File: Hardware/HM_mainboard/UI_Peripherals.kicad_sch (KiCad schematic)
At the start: 20 parts, among them J4 FC68125, U3 WE-TVS-824015043

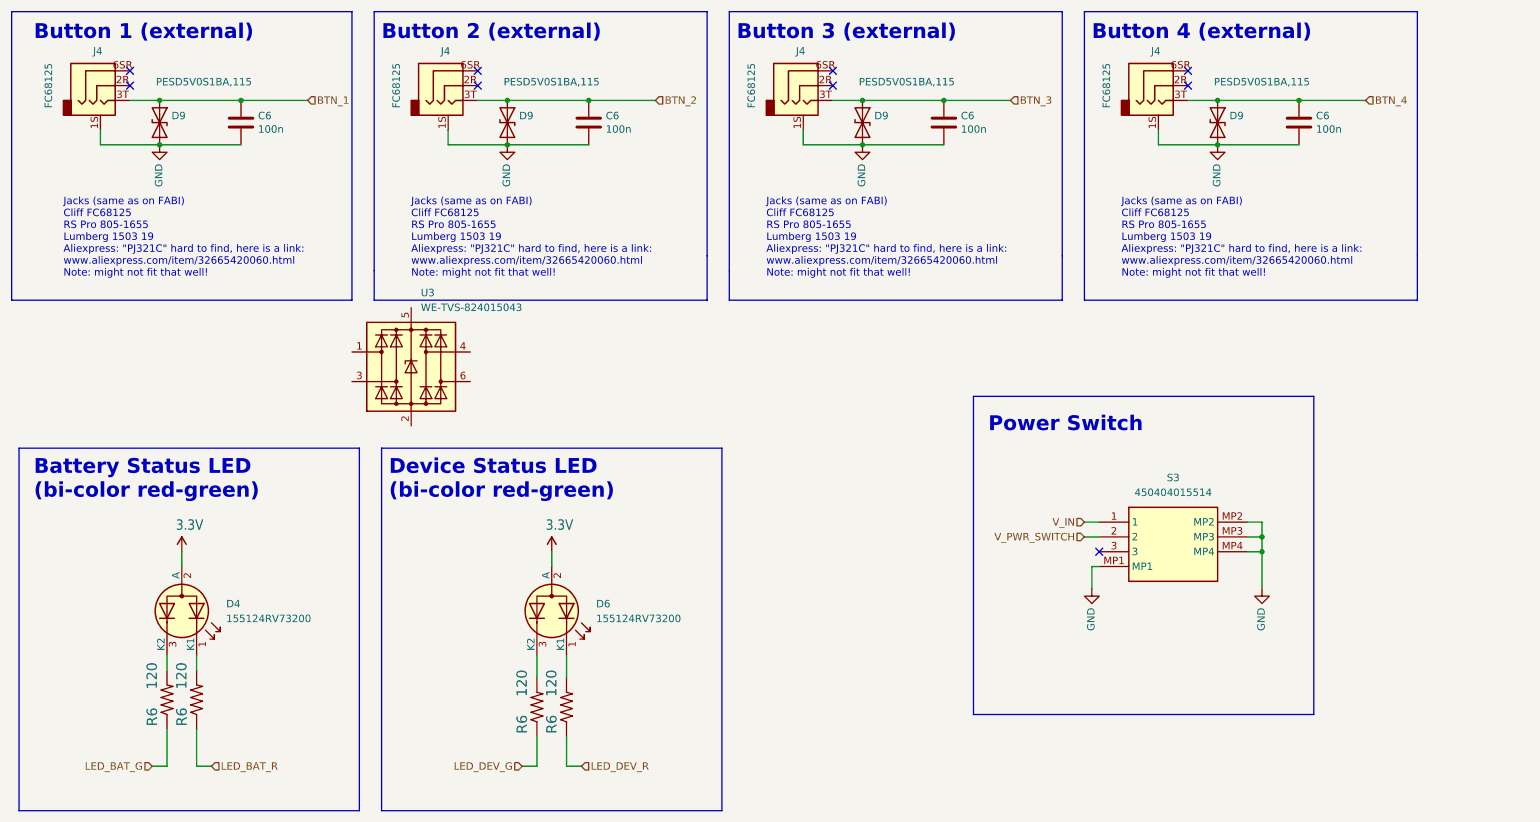
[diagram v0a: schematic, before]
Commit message: Added TVS-Diodes for button jacks
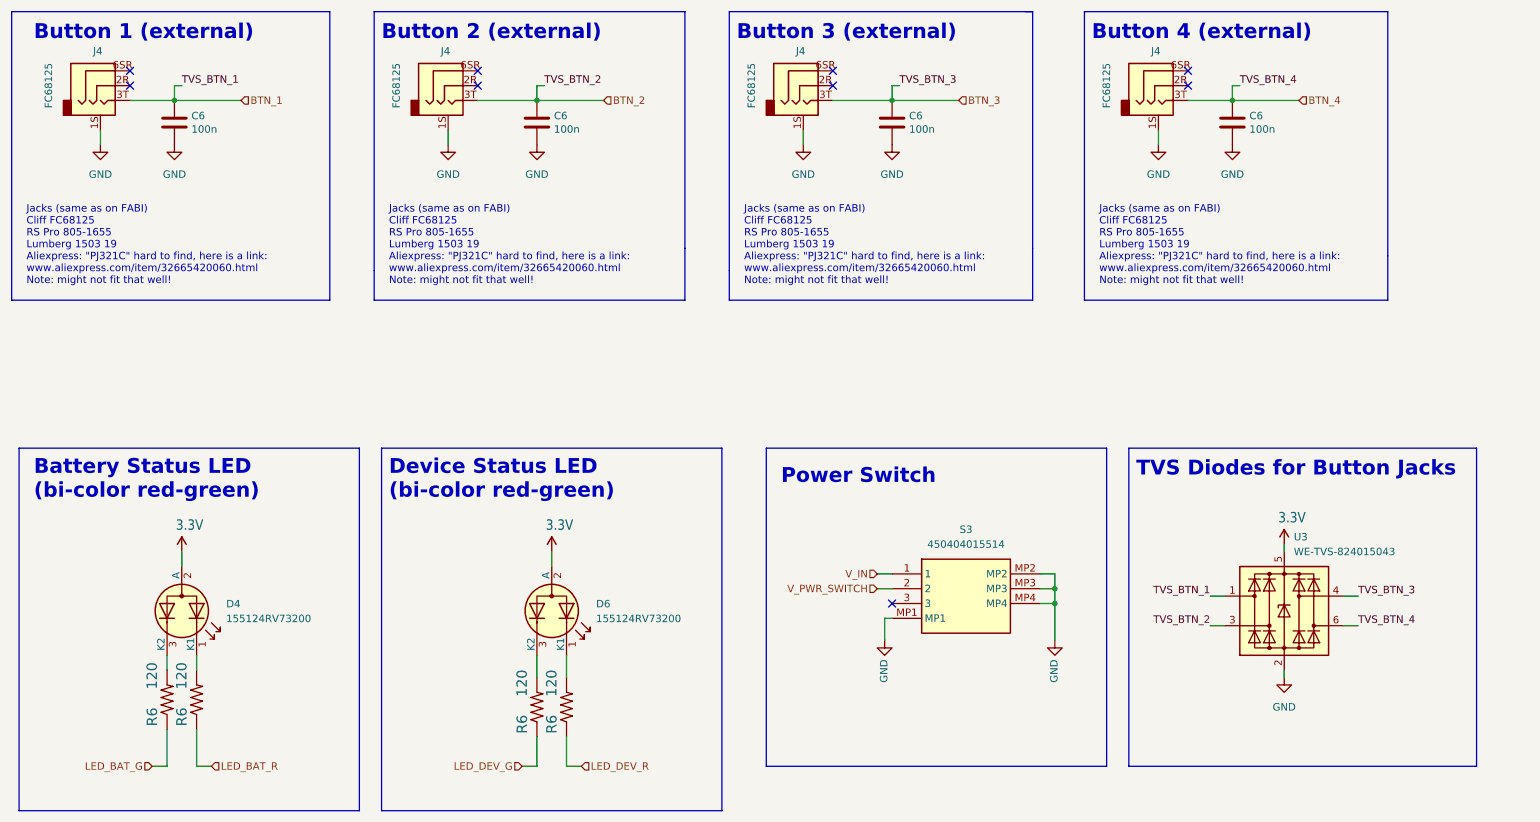
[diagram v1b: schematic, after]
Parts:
- removed D9 (x4): PESD5V0S1BA,115, Diode_SMD:D_SOD-323, symbol Device:D_TVS
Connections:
- net 3.3V: now also U3.5 (VBUS)
- net BTN_1: now also U3.1 (I/O1)
- net BTN_2: now also U3.3 (I/O2)
- net BTN_3: now also U3.4 (I/O3)
- net BTN_4: now also U3.6 (I/O4)
- net GND: now also U3.2 (GND)
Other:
- note added: "TVS Diodes for Button Jacks"
- moved on the sheet: C6, S3, U3

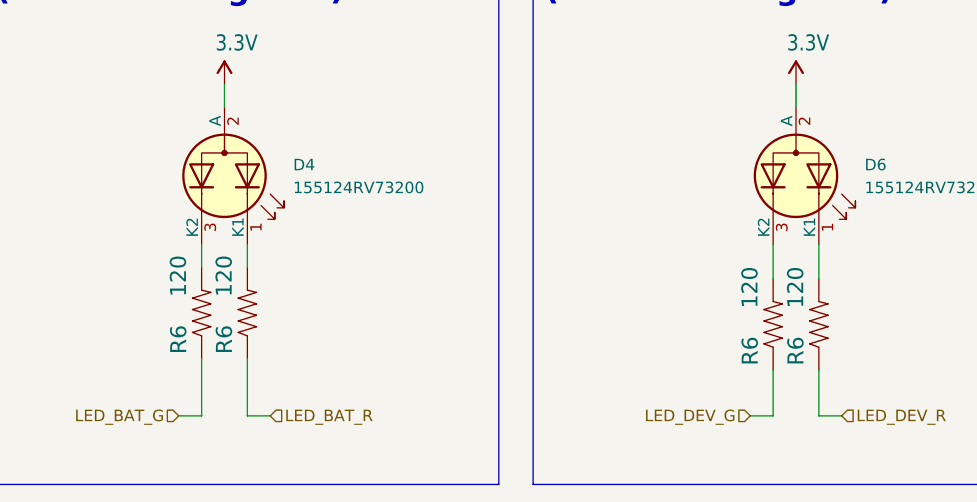
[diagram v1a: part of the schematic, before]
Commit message: Updated components of power supply unit
- Replaced PMOSFET
- Replaced LDO
- Replaced battery charger
- Replaced caps and resistors
- Replaced battery connector
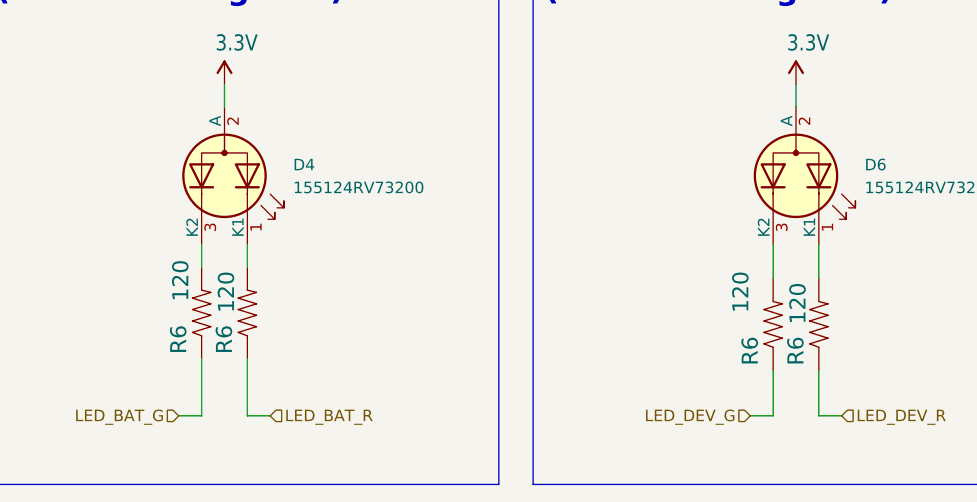
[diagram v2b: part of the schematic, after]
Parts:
- removed R6 (x3): 120, Resistor_SMD:R_0201_0603Metric_Pad0.64x0.40mm_HandSolder, symbol esp32-thing-eagle-import:27OHM1/10W1%(0603)0603-RES
- added R6 (x3): 120, Resistor_SMD:R_0201_0603Metric_Pad0.64x0.40mm_HandSolder, symbol esp32-thing-eagle-import:27OHM1/10W1%(0603)0603-RES
- R6: value 120 -> 120; Mouser (none) -> ERJ-PA3J121V
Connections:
- net LED_BAT_R: now also R6.1
- net LED_DEV_G: now also R6.1
- net LED_DEV_R: now also R6.1
- net at D6.1 (K1): now also R6.2
- net at D6.3 (K2): now also R6.2
- net at D4.1 (K1): now also R6.2
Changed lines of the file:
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@@
       (effects (font (size 1.778 1.778)) (justify left bottom))
     )
-    (property "Value" "120" (at 116.586 151.892 0)
+    (property "Value" "120 " (at 115.57 152.4 0)
       (effects (font (size 1.778 1.778)) (justify left bottom))
     )
@@
       (effects (font (size 1.27 1.27)) hide)
     )
+    (property "Mouser" "ERJ-PA3J121V" (at 118.11 153.67 0)
+      (effects (font (size 1.27 1.27)) hide)
+    )
     (pin "1")
     (pin "2")
@@
         )
         (path "/54a6df43-5475-46a2-9916-8b0260700d4c/137c5701-d01e-40ce-919d-b371cfda41da"
-          (reference "R13") (unit 1)
+          (reference "R6") (unit 1)
         )
       )
@@
     )
   )
+  (symbol (lib_id "esp32-thing-eagle-import:27OHM1/10W1%(0603)0603-RES") (at 59.69 152.4 90) (unit 1)
+    (in_bom yes) (on_board yes) (dnp no)
+    (property "Reference" "R6" (at 58.1914 156.972 0)
+      (effects (font (size 1.778 1.778)) (justify left bottom))
+    )
+    (property "Value" "120 " (at 58.42 152.4 0)
+      (effects (font (size 1.778 1.778)) (justify left bottom))
+    )
+    (property "Footprint" "Resistor_SMD:R_0201_0603Metric_Pad0.64x0.40mm_HandSolder" (at 59.69 152.4 0)
+      (effects (font (size 1.27 1.27)) hide)
+    )
+    (property "Datasheet" "" (at 59.69 152.4 0)
+      (effects (font (size 1.27 1.27)) hide)
+    )
+    (property "Mouser" "ERJ-PA3J121V" (at 59.69 152.4 0)
+      (effects (font (size 1.27 1.27)) hide)
+    )
+    (pin "1")
+    (pin "2")
+    (instances
+      (project "HM_mainboard"
+        (path "/54a6df43-5475-46a2-9916-8b0260700d4c"
+          (reference "R6") (unit 1)
+        )
+        (path "/54a6df43-5475-46a2-9916-8b0260700d4c/8a725ce3-408a-4762-9df2-b56094186e56"
+          (reference "R14") (unit 1)
+        )
+        (path "/54a6df43-5475-46a2-9916-8b0260700d4c/137c5701-d01e-40ce-919d-b371cfda41da"
+          (reference "R5") (unit 1)
+        )
+      )
+      (project "esp32-thing"
+        (path "/64c5aff3-bdec-4fb6-b5ec-87e5efa2adf7"
+          (reference "R13") (unit 1)
+        )
+      )
+    )
+  )
   (symbol (lib_name "GND_1") (lib_id "power:GND") (at 118.11 57.15 0) (unit 1)
     (in_bom yes) (on_board yes) (dnp no) (fields_autoplaced)
@@
       (effects (font (size 1.778 1.778)) (justify left bottom))
     )
-    (property "Value" "120" (at 53.086 150.622 0)
+    (property "Value" "120 " (at 53.34 151.13 0)
       (effects (font (size 1.778 1.778)) (justify left bottom))
     )
@@
     )
     (property "Datasheet" "" (at 54.61 152.4 0)
+      (effects (font (size 1.27 1.27)) hide)
+    )
+    (property "Mouser" "ERJ-PA3J121V" (at 54.61 152.4 0)
       (effects (font (size 1.27 1.27)) hide)
     )
@@
     )
   )
-  (symbol (lib_id "esp32-thing-eagle-import:27OHM1/10W1%(0603)0603-RES") (at 59.69 152.4 90) (unit 1)
-    (in_bom yes) (on_board yes) (dnp no)
-    (property "Reference" "R6" (at 58.1914 156.972 0)
+  (symbol (lib_id "esp32-thing-eagle-import:27OHM1/10W1%(0603)0603-RES") (at 123.19 153.67 90) (unit 1)
+    (in_bom yes) (on_board yes) (dnp no)
+    (property "Reference" "R6" (at 121.6914 158.242 0)
       (effects (font (size 1.778 1.778)) (justify left bottom))
     )
-    (property "Value" "120" (at 58.166 150.622 0)
+    (property "Value" "120 " (at 121.92 153.67 0)
       (effects (font (size 1.778 1.778)) (justify left bottom))
     )
-    (property "Footprint" "Resistor_SMD:R_0201_0603Metric_Pad0.64x0.40mm_HandSolder" (at 59.69 152.4 0)
-      (effects (font (size 1.27 1.27)) hide)
-    )
-    (property "Datasheet" "" (at 59.69 152.4 0)
+    (property "Footprint" "Resistor_SMD:R_0201_0603Metric_Pad0.64x0.40mm_HandSolder" (at 123.19 153.67 0)
+      (effects (font (size 1.27 1.27)) hide)
+    )
+    (property "Datasheet" "" (at 123.19 153.67 0)
+      (effects (font (size 1.27 1.27)) hide)
+    )
+    (property "Mouser" "ERJ-PA3J121V" (at 123.19 153.67 0)
       (effects (font (size 1.27 1.27)) hide)
     )
@@
         )
         (path "/54a6df43-5475-46a2-9916-8b0260700d4c/137c5701-d01e-40ce-919d-b371cfda41da"
-          (reference "R12") (unit 1)
+          (reference "R8") (unit 1)
         )
       )
@@
         )
       )
-    )
-  )
-  (symbol (lib_id "esp32-thing-eagle-import:27OHM1/10W1%(0603)0603-RES") (at 123.19 153.67 90) (unit 1)
-    (in_bom yes) (on_board yes) (dnp no)
-    (property "Reference" "R6" (at 121.6914 158.242 0)
-      (effects (font (size 1.778 1.778)) (justify left bottom))
-    )
-    (property "Value" "120" (at 121.666 151.892 0)
-      (effects (font (size 1.778 1.778)) (justify left bottom))
-    )
-    (property "Footprint" "Resistor_SMD:R_0201_0603Metric_Pad0.64x0.40mm_HandSolder" (at 123.19 153.67 0)
-      (effects (font (size 1.27 1.27)) hide)
-    )
-    (property "Datasheet" "" (at 123.19 153.67 0)
-      (effects (font (size 1.27 1.27)) hide)
-    )
-    (pin "1")
-    (pin "2")
-    (instances
-      (project "HM_mainboard"
-        (path "/54a6df43-5475-46a2-9916-8b0260700d4c"
-          (reference "R6") (unit 1)
-        )
-        (path "/54a6df43-5475-46a2-9916-8b0260700d4c/8a725ce3-408a-4762-9df2-b56094186e56"
-          (reference "R14") (unit 1)
-        )
-        (path "/54a6df43-5475-46a2-9916-8b0260700d4c/137c5701-d01e-40ce-919d-b371cfda41da"
-          (reference "R14") (unit 1)
-        )
-      )
-      (project "esp32-thing"
-        (path "/64c5aff3-bdec-4fb6-b5ec-87e5efa2adf7"
-          (reference "R13") (unit 1)
-        )
-      )
